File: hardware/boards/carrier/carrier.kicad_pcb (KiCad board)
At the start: 4 copper layers, 106 x 34.3 mm, 68 parts, among them J1 XT30PW(2+2), Q1 IPB020N10N5LF, Q2 2N7002, Q3 2N7002, SW1 SKSCLCE010, U1 STM32C092GCU7, U2 LM5163DDAR, U3 LMX5069MS, U4 INA237AIDGSR, U5 TCAN3413DR

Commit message: Update carrier PCB placement
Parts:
- moved TP5 30.9 mm to (108.7, 114.1)
- moved TP17 23.5 mm to (105.3, 113.1)
- moved TP18 23.1 mm to (105.2, 117.1)
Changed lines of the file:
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@@
 				(font
 					(size 1 1)
+					(thickness 0.15)
 				)
 			)
@@
 				(font
 					(size 1 1)
+					(thickness 0.15)
 				)
 			)
@@
 				(font
 					(size 1 1)
+					(thickness 0.15)
 				)
 			)
@@
 	(footprint "TestPoint:TestPoint_Pad_D1.5mm"
 		(layer "B.Cu")
-		(at 91.53619 135.73 180)
+		(at 105.21 117.1 180)
 		(descr "SMD pad as test Point, diameter 1.5mm")
 		(tags "test point SMD pad")
@@
 	(footprint "TestPoint:TestPoint_Pad_D1.5mm"
 		(layer "B.Cu")
-		(at 91.53619 132.18 180)
+		(at 105.34 113.11 180)
 		(descr "SMD pad as test Point, diameter 1.5mm")
 		(tags "test point SMD pad")
@@
 	(footprint "TestPoint:TestPoint_Pad_D1.0mm"
 		(layer "B.Cu")
-		(at 92.12619 140.19 180)
+		(at 108.71 114.11 180)
 		(descr "SMD pad as test Point, diameter 1.0mm")
 		(tags "test point SMD pad")

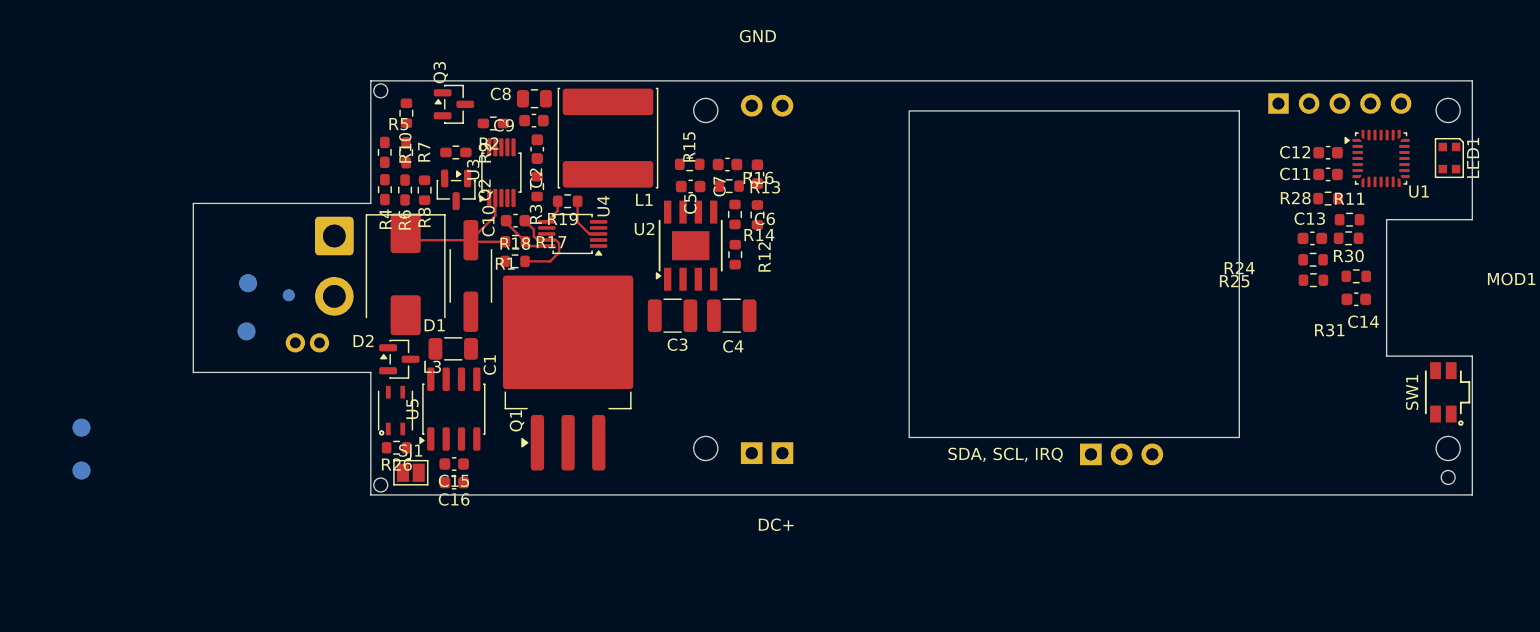
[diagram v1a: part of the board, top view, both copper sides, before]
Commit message: Checkpoint carrier placement updates
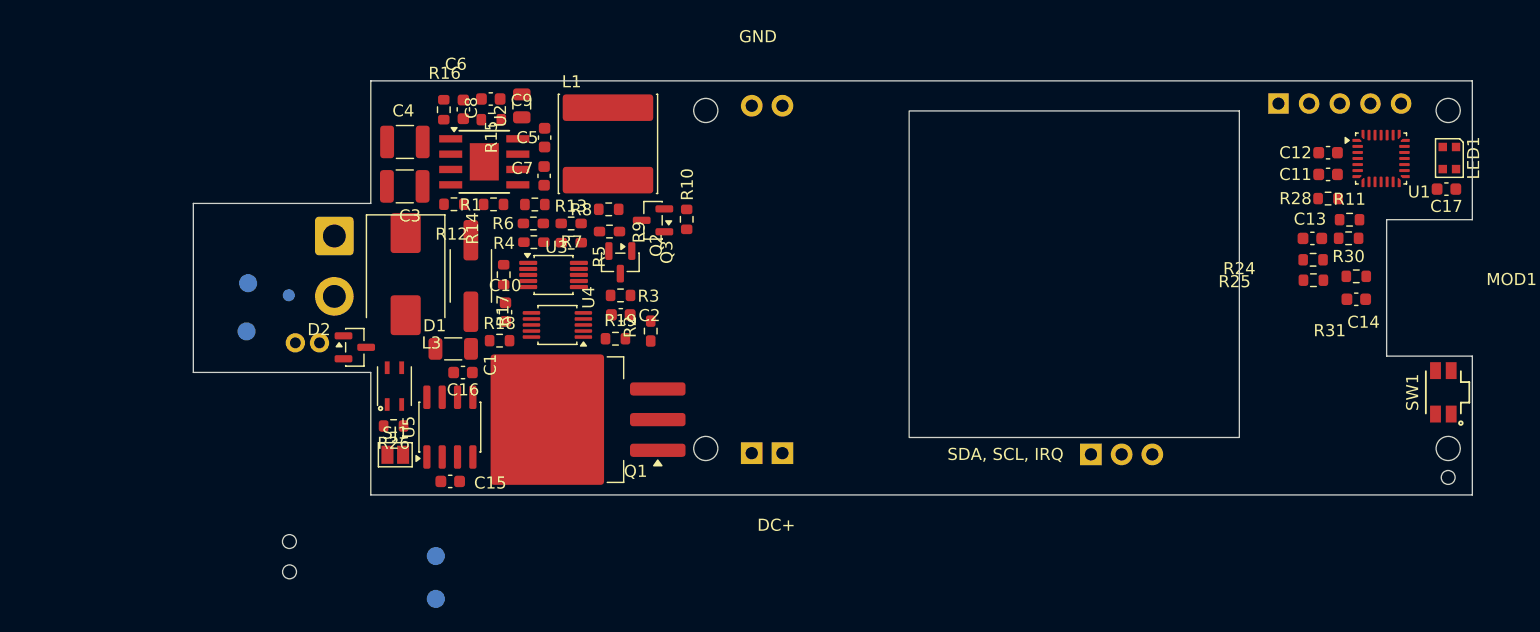
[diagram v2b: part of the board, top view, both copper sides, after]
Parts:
- added C17: 100nF, Capacitor_SMD:C_0603_1608Metric, F.Cu at (204.6, 105.3)
- moved H9 40.6 mm to (108.8, 137.0)
- moved TP6 31.2 mm to (120.9, 135.7)
- moved TP7 31.2 mm to (120.9, 139.3)
- moved C4 30.7 mm to (118.3, 101.4), turned to 180 degrees
- moved R16 27.4 mm to (121.5, 98.7)
- moved C6 24.9 mm to (123.2, 98.7), turned to 90 degrees
- moved R10 24.8 mm to (141.7, 107.8), turned to 90 degrees
- moved C3 24.6 mm to (118.3, 105.1)
- moved R12 23.7 mm to (122.4, 106.6), turned to 0 degrees
- moved R2 21.6 mm to (138.7, 117.1), turned to -90 degrees
- moved R14 20.0 mm to (125.7, 106.6), turned to 180 degrees
- moved Q3 19.1 mm to (138.9, 107.9), turned to 180 degrees
- moved U2 18.5 mm to (124.9, 103.1), turned to 0 degrees
- moved R5 17.2 mm to (132.1, 109.8), turned to 0 degrees
- moved R15 16.8 mm to (125.5, 99.6), turned to 180 degrees
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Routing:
- net VCC: track 12.9 -> 0.00 mm
- net /Protected Power and Controls/INA_INM_FILT: track 7.81 -> 0.00 mm
- net /Protected Power and Controls/INA_INP_FILT: track 4.31 -> 0.00 mm
- net /INA_ALERT: track 3.87 -> 0.00 mm
- net +3V3: track 2.09 -> 0.00 mm

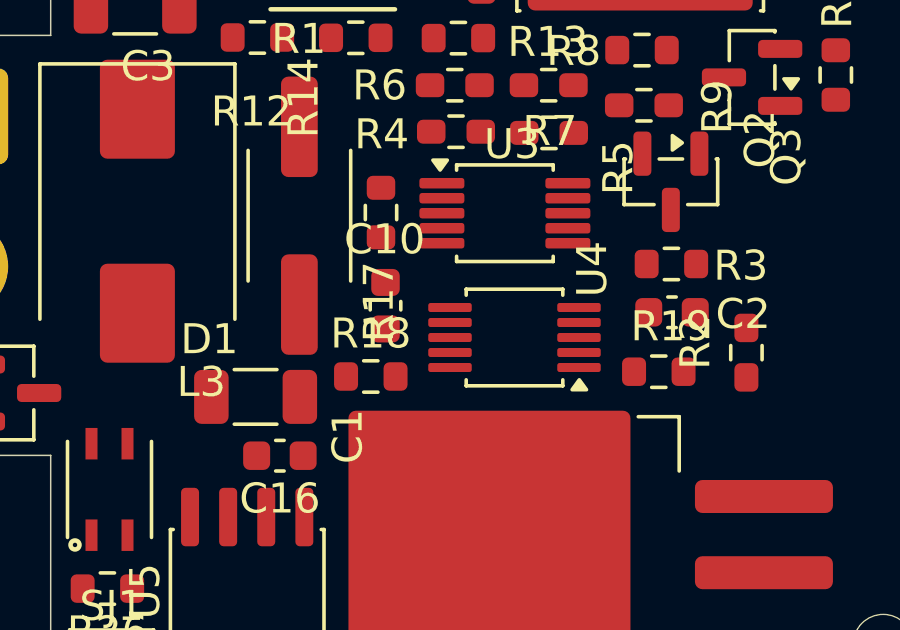
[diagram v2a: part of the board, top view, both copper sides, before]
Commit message: Add INA bypass and CAN differential pair rules
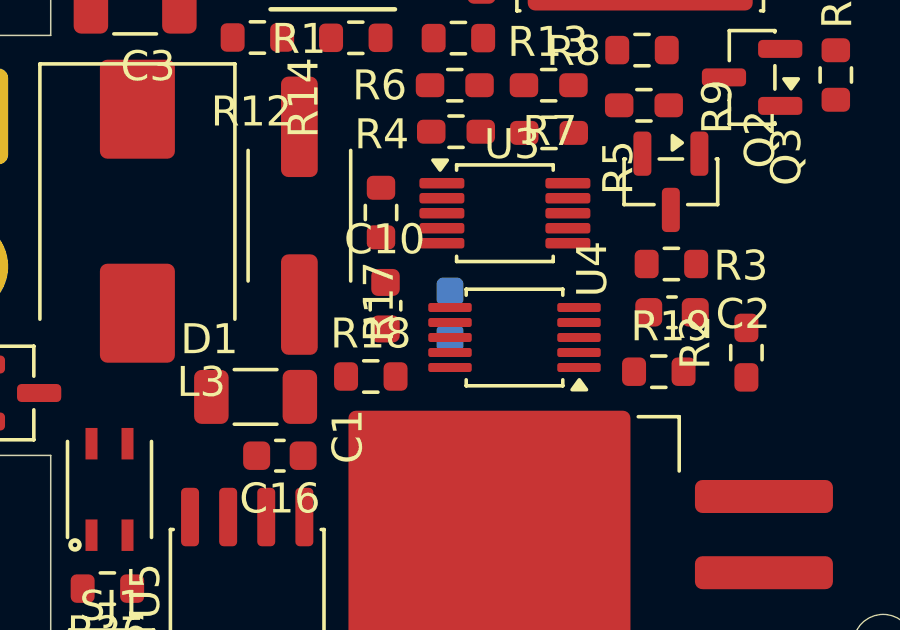
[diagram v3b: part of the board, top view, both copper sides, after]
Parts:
- added C18: 100nF, Capacitor_SMD:C_0603_1608Metric, B.Cu at (128.8, 115.8)
- TP17: value CANH_BUS -> CAN_BUS_P
- TP18: value CANL_BUS -> CAN_BUS_N
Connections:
- net /CANH_BUS renamed /CAN_BUS_P
- net /CANL_BUS renamed /CAN_BUS_N
- net Net-(L3-A_PHY) renamed /Protected Power and Controls/CAN_PHY_P
- net Net-(L3-B_PHY) renamed /Protected Power and Controls/CAN_PHY_N
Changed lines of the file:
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@@
 		)
 	)
+	(footprint "Capacitor_SMD:C_0603_1608Metric"
+		(layer "B.Cu")
+		(at 128.81 115.82 -90)
+		(descr "Capacitor SMD 0603 (1608 Metric), square (rectangular) end terminal, IPC-7351 nominal, (Body size source: IPC-SM-782 page 76, https://www.pcb-3d.com/wordpress/wp-content/uploads/ipc-sm-782a_amendment_1_and_2.pdf)")
+		(tags "capacitor")
+		(property "Reference" "C18"
+			(at 0 2.5 0)
+			(layer "B.SilkS")
+			(effects
+				(font
+					(size 1 1)
+					(thickness 0.15)
+				)
+				(justify mirror)
+			)
+		)
+		(property "Value" "100nF"
+			(at 0 -1.43 0)
+			(layer "B.Fab")
+			(effects
+				(font
+					(size 1 1)
+					(thickness 0.15)
+				)
+				(justify mirror)
+			)
+		)
+		(property "Datasheet" "https://www.ti.com/lit/ds/symlink/ina237.pdf"
+			(at 0 0 0)
+			(layer "B.Fab")
+			(hide yes)
+			(effects
+				(font
+					(size 1.27 1.27)
+				)
+				(justify mirror)
+			)
+		)
+		(property "Description" "INA237 local supply bypass; place directly at U4 pins 6 and 7"
+			(at 0 0 0)
+			(layer "B.Fab")
+			(hide yes)
+			(effects
+				(font
+					(size 1.27 1.27)
+				)
+				(justify mirror)
+			)
+		)
+		(property "KiLib_Generator" "SMD_2terminal_chip_molded"
+			(at 0 0 0)
+			(layer "B.SilkS")
+			(hide yes)
+			(effects
+				(font
+					(size 1 1)
+					(thickness 0.15)
+				)
+				(justify mirror)
+			)
+		)
+		(property ki_fp_filters "C_*")
+		(sheetname "/Protected Power and Controls/")
+		(sheetfile "01_power_control.kicad_sch")
+		(units
+			(unit
+				(name "A")
+				(pins "1" "2")
+			)
+		)
+		(attr smd)
+		(duplicate_pad_numbers_are_jumpers no)
+		(fp_line
+			(start -0.14058 0.51)
+			(end 0.14058 0.51)
+			(stroke
+				(width 0.12)
+				(type solid)
+			)
+			(layer "B.SilkS")
+		)
+		(fp_line
+			(start -0.14058 -0.51)
+			(end 0.14058 -0.51)
+			(stroke
+				(width 0.12)
+				(type solid)
+			)
+			(layer "B.SilkS")
+		)
+		(fp_rect
+			(start -1.48 -0.73)
+			(end 1.48 0.73)
+			(stroke
+				(width 0.05)
+				(type solid)
+			)
+			(fill no)
+			(layer "B.CrtYd")
+		)
+		(fp_rect
+			(start -0.8 -0.4)
+			(end 0.8 0.4)
+			(stroke
+				(width 0.1)
+				(type solid)
+			)
+			(fill no)
+			(layer "B.Fab")
+		)
+		(fp_text user "${REFERENCE}"
+			(at 0 0 0)
+			(layer "B.Fab")
+			(effects
+				(font
+					(size 0.4 0.4)
+					(thickness 0.06)
+				)
+				(justify mirror)
+			)
+		)
+		(pad "1" smd roundrect
+			(at -0.775 0 180)
+			(size 0.9 0.95)
+			(layers "B.Cu" "B.Mask" "B.Paste")
+			(roundrect_rratio 0.25)
+			(net "+3V3")
+			(pintype "passive")
+		)
+		(pad "2" smd roundrect
+			(at 0.775 0 180)
+			(size 0.9 0.95)
+			(layers "B.Cu" "B.Mask" "B.Paste")
+			(roundrect_rratio 0.25)
+			(net "GND")
+			(pintype "passive")
+		)
+		(embedded_fonts no)
+		(model "${KICAD10_3DMODEL_DIR}/Capacitor_SMD.3dshapes/C_0603_1608Metric.step"
+			(offset
+				(xyz 0 0 0)
+			)
+			(scale
+				(xyz 1 1 1)
+			)
+			(rotate
+				(xyz 0 0 0)
+			)
+		)
+	)
 	(footprint "Resistor_SMD:R_0603_1608Metric"
 		(layer "F.Cu")
@@
 			(size 1 1.5)
 			(layers "F.Cu" "F.Mask")
-			(net "/CANH_BUS")
+			(net "/CAN_BUS_P")
 			(pinfunction "A_1")
 			(pintype "passive")
@@
 			(layers "*.Cu" "*.Mask")
 			(remove_unused_layers no)
-			(net "/CANL_BUS")
+			(net "/CAN_BUS_N")
 			(pinfunction "Pin_3_3")
 			(pintype "passive")
@@
 			(layers "*.Cu" "*.Mask")
 			(remove_unused_layers no)
-			(net "/CANH_BUS")
+			(net "/CAN_BUS_P")
 			(pinfunction "Pin_4_4")
 			(pintype "passive")
@@
 			(layers "F.Cu" "F.Mask" "F.Paste")
 			(roundrect_rratio 0.25)
-			(net "/CANL_BUS")
+			(net "/CAN_BUS_N")
 			(pintype "passive")
 		)
@@
 			(size 1.05 0.4)
 			(layers "F.Cu" "F.Mask" "F.Paste")
-			(net "Net-(L3-A_PHY)")
+			(net "/Protected Power and Controls/CAN_PHY_P")
 			(pinfunction "A_PHY_1")
 			(pintype "passive")
@@
 			(size 1.05 0.4)
 			(layers "F.Cu" "F.Mask" "F.Paste")
-			(net "Net-(L3-B_PHY)")
+			(net "/Protected Power and Controls/CAN_PHY_N")
 			(pinfunction "B_PHY_2")
 			(pintype "passive")
@@
 			(size 1.05 0.4)
 			(layers "F.Cu" "F.Mask" "F.Paste")
-			(net "/CANL_BUS")
+			(net "/CAN_BUS_N")
 			(pinfunction "B_BUS_3")
 			(pintype "passive")
@@
 			(size 1.05 0.4)
 			(layers "F.Cu" "F.Mask" "F.Paste")
-			(net "/CANH_BUS")
+			(net "/CAN_BUS_P")
 			(pinfunction "A_BUS_4")
 			(pintype "passive")
@@
 			(layers "F.Cu" "F.Mask" "F.Paste")
 			(roundrect_rratio 0.25)
-			(net "/CANH_BUS")
+			(net "/CAN_BUS_P")
 			(pinfunction "IO1_1")
 			(pintype "passive")
@@
 			(layers "F.Cu" "F.Mask" "F.Paste")
 			(roundrect_rratio 0.25)
-			(net "/CANL_BUS")
+			(net "/CAN_BUS_N")
 			(pinfunction "IO2_2")
 			(pintype "passive")
@@
 			(layers "F.Cu" "F.Mask" "F.Paste")
 			(roundrect_rratio 0.25)
-			(net "Net-(L3-B_PHY)")
+			(net "/Protected Power and Controls/CAN_PHY_N")
 			(pinfunction "CANL_6")
 			(pintype "bidirectional")
@@
 			(layers "F.Cu" "F.Mask" "F.Paste")
 			(roundrect_rratio 0.25)
-			(net "Net-(L3-A_PHY)")
+			(net "/Protected Power and Controls/CAN_PHY_P")
 			(pinfunction "CANH_7")
 			(pintype "bidirectional")
@@
 			)
 		)
-		(property "Value" "CANL_BUS"
+		(property "Value" "CAN_BUS_N"
 			(at 0 -1.75 0)
 			(layer "B.Fab")
@@
 			(size 1.5 1.5)
 			(layers "B.Cu" "B.Mask")
-			(net "/CANL_BUS")
+			(net "/CAN_BUS_N")
 			(pinfunction "1_1")
 			(pintype "passive")
@@
 			)
 		)
-		(property "Value" "CANH_BUS"
+		(property "Value" "CAN_BUS_P"
 			(at 0 -1.75 0)
 			(layer "B.Fab")
@@
 			(size 1.5 1.5)
 			(layers "B.Cu" "B.Mask")
-			(net "/CANH_BUS")
+			(net "/CAN_BUS_P")
 			(pinfunction "1_1")
 			(pintype "passive")

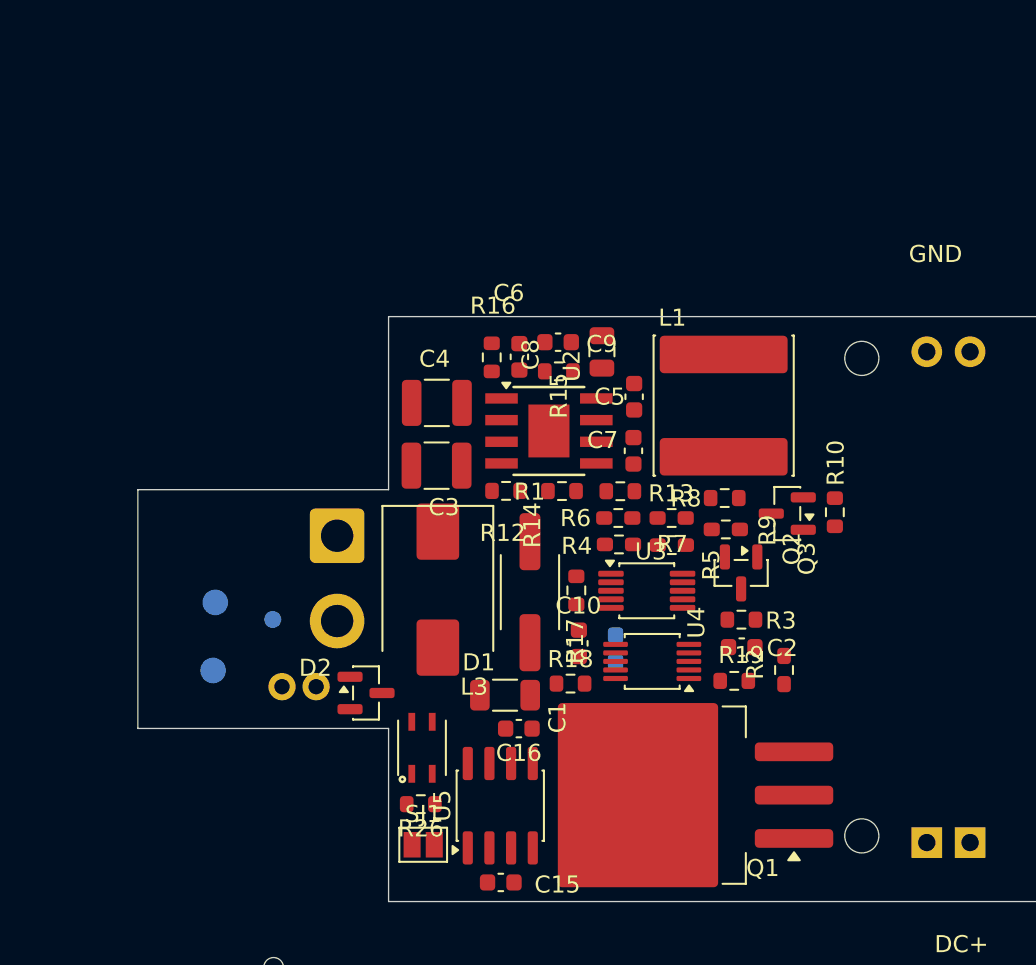
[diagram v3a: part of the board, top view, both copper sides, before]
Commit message: Checkpoint carrier layout edits
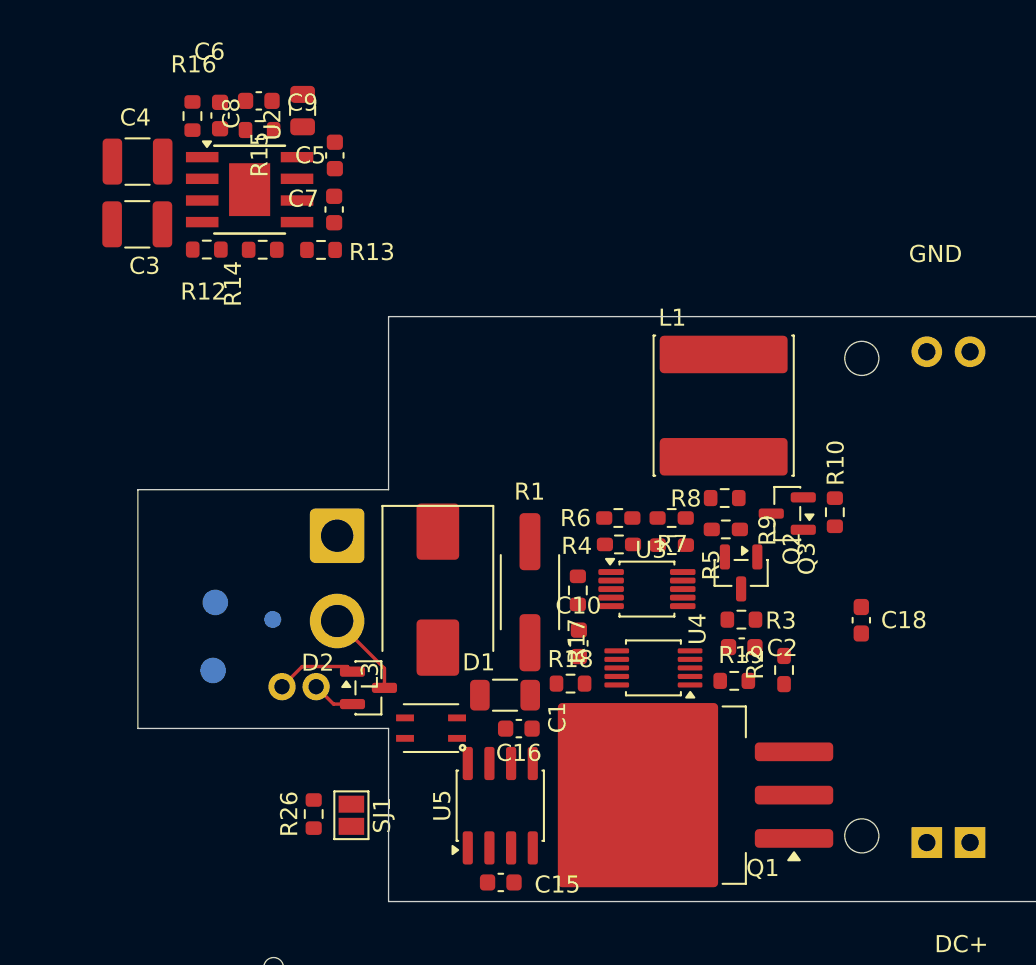
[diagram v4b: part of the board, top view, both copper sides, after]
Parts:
- C18: moved to F.Cu
- moved C7 22.5 mm to (112.3, 90.1)
- moved C5 22.5 mm to (112.3, 86.9)
- moved C3 22.5 mm to (100.8, 90.9)
- moved C8 22.5 mm to (110.5, 84.3)
- moved R13 22.5 mm to (111.5, 92.4)
- moved R15 22.5 mm to (107.9, 85.4)
- moved U2 22.5 mm to (107.4, 88.9)
- moved C4 22.5 mm to (100.8, 87.3)
- moved C6 22.5 mm to (105.6, 84.6)
- moved C9 22.5 mm to (107.9, 83.7)
- moved R12 22.5 mm to (104.8, 92.4)
- moved R14 22.5 mm to (108.1, 92.4)
- moved R16 22.5 mm to (104.0, 84.6)
- moved C18 14.5 mm to (143.2, 114.2)
- moved R26 6.31 mm to (111.1, 125.5), turned to 90 degrees
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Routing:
- net GND: track 0.00 -> 5.07 mm
- net /CAN_BUS_P: track 0.00 -> 4.74 mm
- net /CAN_BUS_N: track 0.00 -> 2.55 mm
